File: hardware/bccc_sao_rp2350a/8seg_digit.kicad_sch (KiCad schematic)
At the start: 11 parts

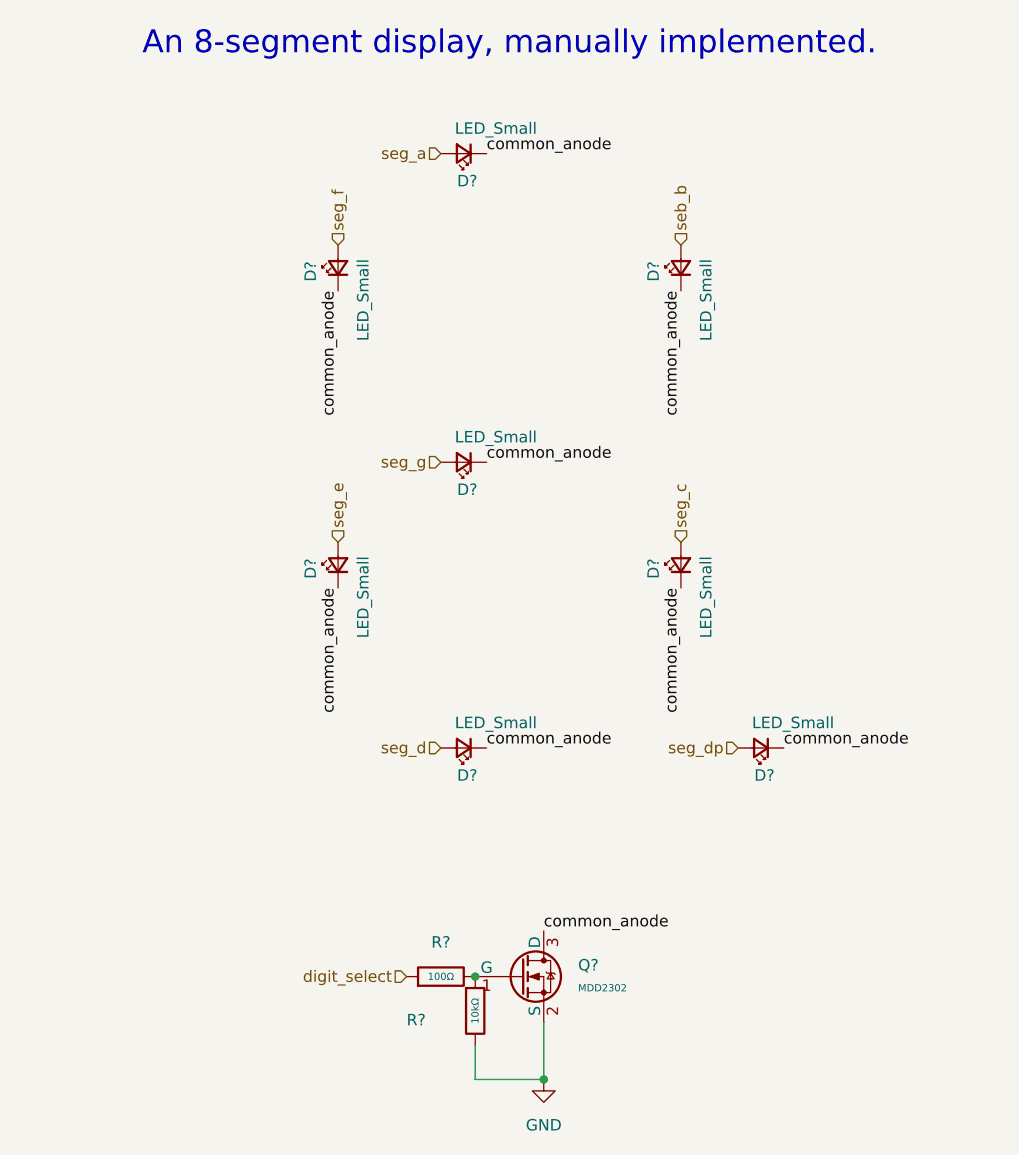
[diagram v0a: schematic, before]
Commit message: hardware edits, changed LED resistor 470->220 ohm, more 'documentation' on board
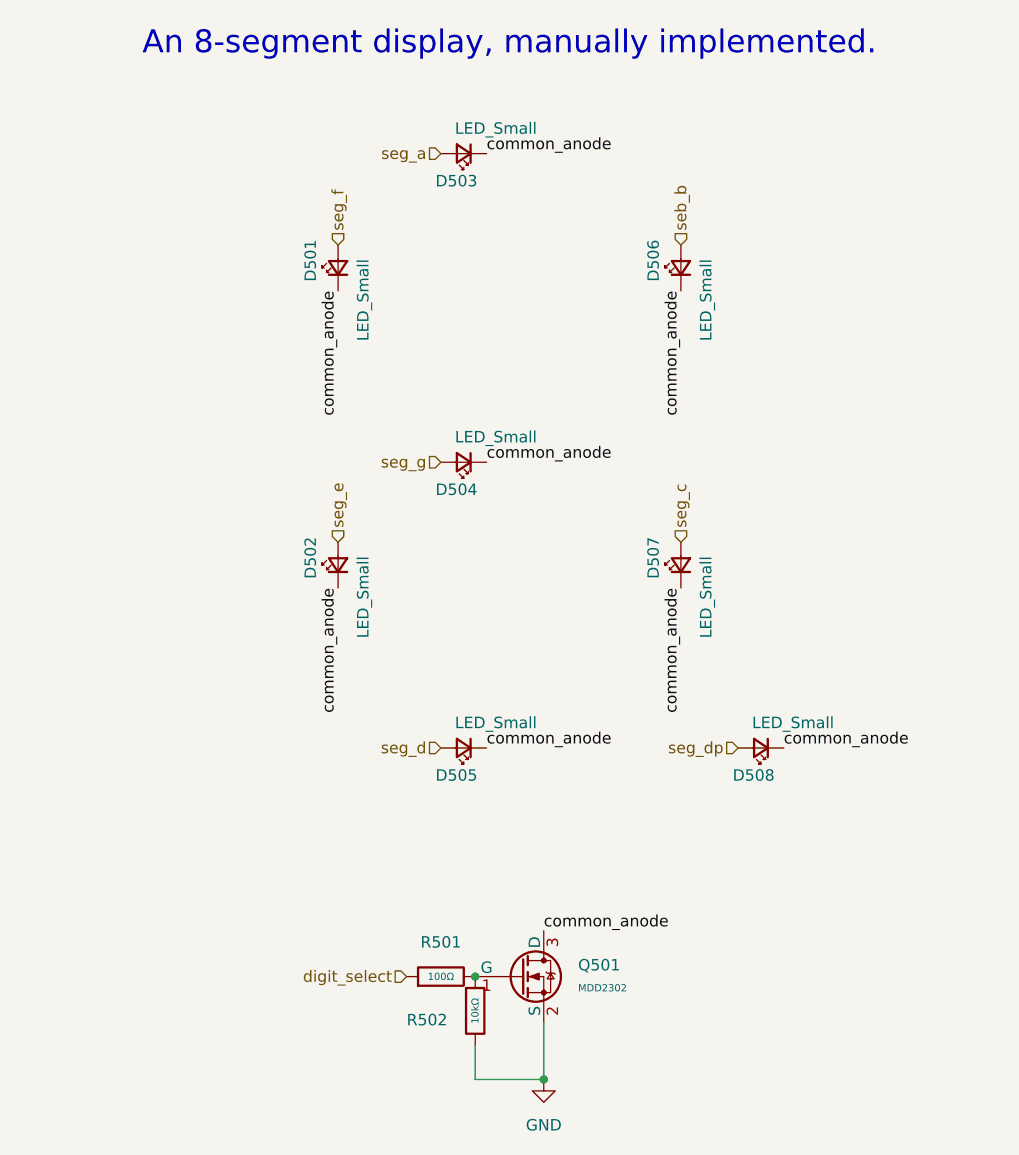
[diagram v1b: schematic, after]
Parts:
- gave numbers to parts that had none: 11
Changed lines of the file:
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@@
 		(on_board yes)
 		(dnp no)
-		(property "Reference" "D?"
+		(property "Reference" "D507"
 			(at 137.922 109.474 0)
 			(effects
@@
 			(project "bccc_sao_rp2350a"
 				(path "/94683f5c-9cd9-448e-be96-9792537b5cb8/9d3d1067-727a-4b8d-8ff8-10c611ad47f2/3b43b8f2-e7a0-488b-8518-96b0bd2c691c"
-					(reference "D?")
+					(reference "D707")
 					(unit 1)
 				)
 				(path "/94683f5c-9cd9-448e-be96-9792537b5cb8/9d3d1067-727a-4b8d-8ff8-10c611ad47f2/47985d3b-a228-40d4-8321-b5efd73f007d"
-					(reference "D?")
+					(reference "D507")
 					(unit 1)
 				)
 				(path "/94683f5c-9cd9-448e-be96-9792537b5cb8/9d3d1067-727a-4b8d-8ff8-10c611ad47f2/c3a468f1-60a1-4701-a354-cffdaea61b57"
-					(reference "D?")
+					(reference "D607")
 					(unit 1)
 				)
@@
 		(dnp no)
 		(fields_autoplaced yes)
-		(property "Reference" "#PWR?"
+		(property "Reference" "#PWR0501"
 			(at 125.73 171.45 0)
 			(effects
@@
 			(project "bccc_sao_rp2350a"
 				(path "/94683f5c-9cd9-448e-be96-9792537b5cb8/9d3d1067-727a-4b8d-8ff8-10c611ad47f2/3b43b8f2-e7a0-488b-8518-96b0bd2c691c"
-					(reference "#PWR?")
+					(reference "#PWR0701")
 					(unit 1)
 				)
 				(path "/94683f5c-9cd9-448e-be96-9792537b5cb8/9d3d1067-727a-4b8d-8ff8-10c611ad47f2/47985d3b-a228-40d4-8321-b5efd73f007d"
-					(reference "#PWR?")
+					(reference "#PWR0501")
 					(unit 1)
 				)
 				(path "/94683f5c-9cd9-448e-be96-9792537b5cb8/9d3d1067-727a-4b8d-8ff8-10c611ad47f2/c3a468f1-60a1-4701-a354-cffdaea61b57"
-					(reference "#PWR?")
+					(reference "#PWR0601")
 					(unit 1)
 				)
@@
 		(on_board yes)
 		(dnp no)
-		(property "Reference" "D?"
+		(property "Reference" "D506"
 			(at 137.922 76.454 0)
 			(effects
@@
 			(project "bccc_sao_rp2350a"
 				(path "/94683f5c-9cd9-448e-be96-9792537b5cb8/9d3d1067-727a-4b8d-8ff8-10c611ad47f2/3b43b8f2-e7a0-488b-8518-96b0bd2c691c"
-					(reference "D?")
+					(reference "D706")
 					(unit 1)
 				)
 				(path "/94683f5c-9cd9-448e-be96-9792537b5cb8/9d3d1067-727a-4b8d-8ff8-10c611ad47f2/47985d3b-a228-40d4-8321-b5efd73f007d"
-					(reference "D?")
+					(reference "D506")
 					(unit 1)
 				)
 				(path "/94683f5c-9cd9-448e-be96-9792537b5cb8/9d3d1067-727a-4b8d-8ff8-10c611ad47f2/c3a468f1-60a1-4701-a354-cffdaea61b57"
-					(reference "D?")
+					(reference "D606")
 					(unit 1)
 				)
@@
 		(on_board yes)
 		(dnp no)
-		(property "Reference" "D?"
+		(property "Reference" "D508"
 			(at 151.384 131.318 0)
 			(effects
@@
 			(project "bccc_sao_rp2350a"
 				(path "/94683f5c-9cd9-448e-be96-9792537b5cb8/9d3d1067-727a-4b8d-8ff8-10c611ad47f2/3b43b8f2-e7a0-488b-8518-96b0bd2c691c"
-					(reference "D?")
+					(reference "D708")
 					(unit 1)
 				)
 				(path "/94683f5c-9cd9-448e-be96-9792537b5cb8/9d3d1067-727a-4b8d-8ff8-10c611ad47f2/47985d3b-a228-40d4-8321-b5efd73f007d"
-					(reference "D?")
+					(reference "D508")
 					(unit 1)
 				)
 				(path "/94683f5c-9cd9-448e-be96-9792537b5cb8/9d3d1067-727a-4b8d-8ff8-10c611ad47f2/c3a468f1-60a1-4701-a354-cffdaea61b57"
-					(reference "D?")
+					(reference "D608")
 					(unit 1)
 				)
@@
 		(on_board yes)
 		(dnp no)
-		(property "Reference" "R?"
+		(property "Reference" "R502"
 			(at 110.49 158.496 0)
 			(effects
@@
 			(project "bccc_sao_rp2350a"
 				(path "/94683f5c-9cd9-448e-be96-9792537b5cb8/9d3d1067-727a-4b8d-8ff8-10c611ad47f2/3b43b8f2-e7a0-488b-8518-96b0bd2c691c"
-					(reference "R?")
+					(reference "R702")
 					(unit 1)
 				)
 				(path "/94683f5c-9cd9-448e-be96-9792537b5cb8/9d3d1067-727a-4b8d-8ff8-10c611ad47f2/47985d3b-a228-40d4-8321-b5efd73f007d"
-					(reference "R?")
+					(reference "R502")
 					(unit 1)
 				)
 				(path "/94683f5c-9cd9-448e-be96-9792537b5cb8/9d3d1067-727a-4b8d-8ff8-10c611ad47f2/c3a468f1-60a1-4701-a354-cffdaea61b57"
-					(reference "R?")
+					(reference "R602")
 					(unit 1)
 				)
@@
 		(on_board yes)
 		(dnp no)
-		(property "Reference" "D?"
+		(property "Reference" "D503"
 			(at 118.364 65.278 0)
 			(effects
@@
 			(project "bccc_sao_rp2350a"
 				(path "/94683f5c-9cd9-448e-be96-9792537b5cb8/9d3d1067-727a-4b8d-8ff8-10c611ad47f2/3b43b8f2-e7a0-488b-8518-96b0bd2c691c"
-					(reference "D?")
+					(reference "D703")
 					(unit 1)
 				)
 				(path "/94683f5c-9cd9-448e-be96-9792537b5cb8/9d3d1067-727a-4b8d-8ff8-10c611ad47f2/47985d3b-a228-40d4-8321-b5efd73f007d"
-					(reference "D?")
+					(reference "D503")
 					(unit 1)
 				)
 				(path "/94683f5c-9cd9-448e-be96-9792537b5cb8/9d3d1067-727a-4b8d-8ff8-10c611ad47f2/c3a468f1-60a1-4701-a354-cffdaea61b57"
-					(reference "D?")
+					(reference "D603")
 					(unit 1)
 				)
@@
 		(dnp no)
 		(fields_autoplaced yes)
-		(property "Reference" "Q?"
+		(property "Reference" "Q501"
 			(at 129.54 152.3999 0)
 			(effects
@@
 			(project "bccc_sao_rp2350a"
 				(path "/94683f5c-9cd9-448e-be96-9792537b5cb8/9d3d1067-727a-4b8d-8ff8-10c611ad47f2/3b43b8f2-e7a0-488b-8518-96b0bd2c691c"
-					(reference "Q?")
+					(reference "Q701")
 					(unit 1)
 				)
 				(path "/94683f5c-9cd9-448e-be96-9792537b5cb8/9d3d1067-727a-4b8d-8ff8-10c611ad47f2/47985d3b-a228-40d4-8321-b5efd73f007d"
-					(reference "Q?")
+					(reference "Q501")
 					(unit 1)
 				)
 				(path "/94683f5c-9cd9-448e-be96-9792537b5cb8/9d3d1067-727a-4b8d-8ff8-10c611ad47f2/c3a468f1-60a1-4701-a354-cffdaea61b57"
-					(reference "Q?")
+					(reference "Q601")
 					(unit 1)
 				)
@@
 		(on_board yes)
 		(dnp no)
-		(property "Reference" "D?"
+		(property "Reference" "D505"
 			(at 118.364 131.318 0)
 			(effects
@@
 			(project "bccc_sao_rp2350a"
 				(path "/94683f5c-9cd9-448e-be96-9792537b5cb8/9d3d1067-727a-4b8d-8ff8-10c611ad47f2/3b43b8f2-e7a0-488b-8518-96b0bd2c691c"
-					(reference "D?")
+					(reference "D705")
 					(unit 1)
 				)
 				(path "/94683f5c-9cd9-448e-be96-9792537b5cb8/9d3d1067-727a-4b8d-8ff8-10c611ad47f2/47985d3b-a228-40d4-8321-b5efd73f007d"
-					(reference "D?")
+					(reference "D505")
 					(unit 1)
 				)
 				(path "/94683f5c-9cd9-448e-be96-9792537b5cb8/9d3d1067-727a-4b8d-8ff8-10c611ad47f2/c3a468f1-60a1-4701-a354-cffdaea61b57"
-					(reference "D?")
+					(reference "D605")
 					(unit 1)
 				)
@@
 		(on_board yes)
 		(dnp no)
-		(property "Reference" "D?"
+		(property "Reference" "D504"
 			(at 118.364 99.568 0)
 			(effects
@@
 			(project "bccc_sao_rp2350a"
 				(path "/94683f5c-9cd9-448e-be96-9792537b5cb8/9d3d1067-727a-4b8d-8ff8-10c611ad47f2/3b43b8f2-e7a0-488b-8518-96b0bd2c691c"
-					(reference "D?")
+					(reference "D704")
 					(unit 1)
 				)
 				(path "/94683f5c-9cd9-448e-be96-9792537b5cb8/9d3d1067-727a-4b8d-8ff8-10c611ad47f2/47985d3b-a228-40d4-8321-b5efd73f007d"
-					(reference "D?")
+					(reference "D504")
 					(unit 1)
 				)
 				(path "/94683f5c-9cd9-448e-be96-9792537b5cb8/9d3d1067-727a-4b8d-8ff8-10c611ad47f2/c3a468f1-60a1-4701-a354-cffdaea61b57"
-					(reference "D?")
+					(reference "D604")
 					(unit 1)
 				)
@@
 		(on_board yes)
 		(dnp no)
-		(property "Reference" "D?"
+		(property "Reference" "D502"
 			(at 99.822 109.474 0)
 			(effects
@@
 			(project "bccc_sao_rp2350a"
 				(path "/94683f5c-9cd9-448e-be96-9792537b5cb8/9d3d1067-727a-4b8d-8ff8-10c611ad47f2/3b43b8f2-e7a0-488b-8518-96b0bd2c691c"
-					(reference "D?")
+					(reference "D702")
 					(unit 1)
 				)
 				(path "/94683f5c-9cd9-448e-be96-9792537b5cb8/9d3d1067-727a-4b8d-8ff8-10c611ad47f2/47985d3b-a228-40d4-8321-b5efd73f007d"
-					(reference "D?")
+					(reference "D502")
 					(unit 1)
 				)
 				(path "/94683f5c-9cd9-448e-be96-9792537b5cb8/9d3d1067-727a-4b8d-8ff8-10c611ad47f2/c3a468f1-60a1-4701-a354-cffdaea61b57"
-					(reference "D?")
+					(reference "D602")
 					(unit 1)
 				)
@@
 		(on_board yes)
 		(dnp no)
-		(property "Reference" "D?"
+		(property "Reference" "D501"
 			(at 99.822 76.454 0)
 			(effects
@@
 			(project "bccc_sao_rp2350a"
 				(path "/94683f5c-9cd9-448e-be96-9792537b5cb8/9d3d1067-727a-4b8d-8ff8-10c611ad47f2/3b43b8f2-e7a0-488b-8518-96b0bd2c691c"
-					(reference "D?")
+					(reference "D701")
 					(unit 1)
 				)
 				(path "/94683f5c-9cd9-448e-be96-9792537b5cb8/9d3d1067-727a-4b8d-8ff8-10c611ad47f2/47985d3b-a228-40d4-8321-b5efd73f007d"
-					(reference "D?")
+					(reference "D501")
 					(unit 1)
 				)
 				(path "/94683f5c-9cd9-448e-be96-9792537b5cb8/9d3d1067-727a-4b8d-8ff8-10c611ad47f2/c3a468f1-60a1-4701-a354-cffdaea61b57"
-					(reference "D?")
+					(reference "D601")
 					(unit 1)
 				)
@@
 		(dnp no)
 		(fields_autoplaced yes)
-		(property "Reference" "R?"
+		(property "Reference" "R501"
 			(at 114.3 149.86 90)
 			(effects
@@
 			(project "bccc_sao_rp2350a"
 				(path "/94683f5c-9cd9-448e-be96-9792537b5cb8/9d3d1067-727a-4b8d-8ff8-10c611ad47f2/3b43b8f2-e7a0-488b-8518-96b0bd2c691c"
-					(reference "R?")
+					(reference "R701")
 					(unit 1)
 				)
 				(path "/94683f5c-9cd9-448e-be96-9792537b5cb8/9d3d1067-727a-4b8d-8ff8-10c611ad47f2/47985d3b-a228-40d4-8321-b5efd73f007d"
-					(reference "R?")
+					(reference "R501")
 					(unit 1)
 				)
 				(path "/94683f5c-9cd9-448e-be96-9792537b5cb8/9d3d1067-727a-4b8d-8ff8-10c611ad47f2/c3a468f1-60a1-4701-a354-cffdaea61b57"
-					(reference "R?")
-					(unit 1)
-				)
+					(reference "R601")
+					(unit 1)
+				)
